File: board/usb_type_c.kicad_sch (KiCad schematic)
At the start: 3 parts, among them J1101 MOLEX_2171790001, U1101 DT1446-04V-7

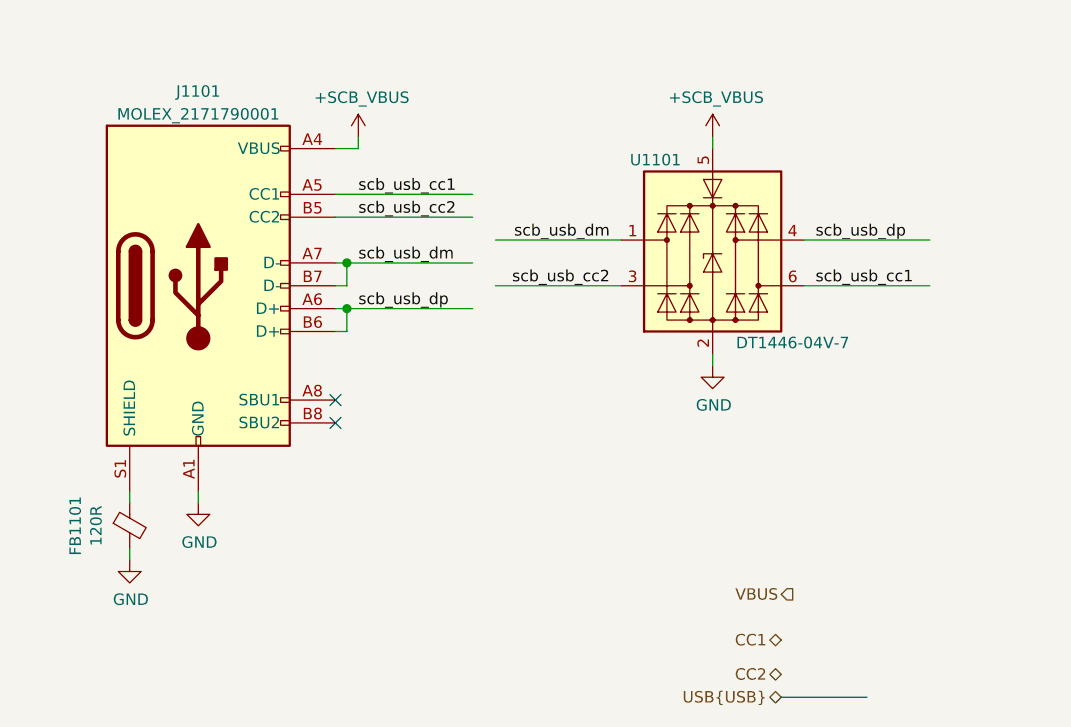
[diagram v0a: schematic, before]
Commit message: Added testpoints and other fixes
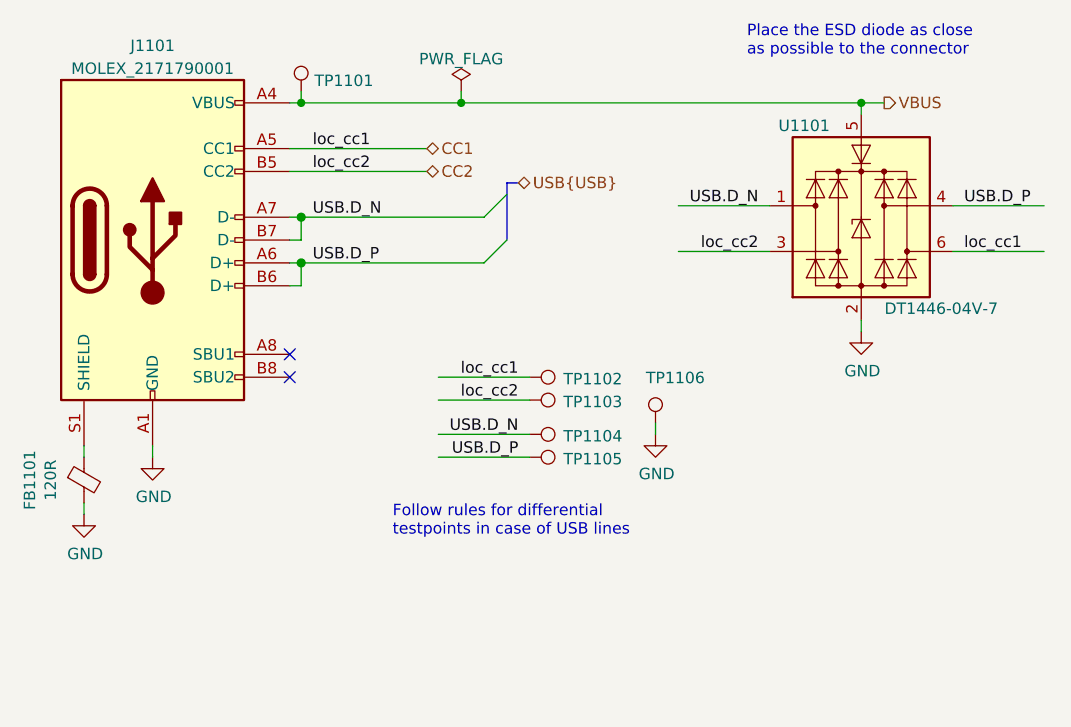
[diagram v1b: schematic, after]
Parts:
- added TP1101, TP1102, TP1103, TP1104, TP1105, TP1106: TestPoint, DIYPie:TestPoint_Pad_D1.5mm, symbol DIYPie:TestPoint
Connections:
- net +5V is gone; now on net VBUS: J1101.A4 (VBUS), J1101.A9 (VBUS), J1101.B4 (VBUS), J1101.B9 (VBUS), U1101.5 (VBUS)
- net scb_usb_cc1 is gone; now on net CC1: J1101.A5 (CC1), U1101.6 (I/O4)
- net scb_usb_cc2 is gone; now on net CC2: J1101.B5 (CC2), U1101.3 (I/O2)
- net CC1: now also TP1102.1
- net CC2: now also TP1103.1
- net GND: now also TP1106.1
- net VBUS: now also TP1101.1
- net scb_usb_dm renamed USB.D_N
- net USB.D_N: now also TP1104.1
- net scb_usb_dp renamed USB.D_P
- net USB.D_P: now also TP1105.1
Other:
- note added: "Follow rules for differential testpoints in case of USB lines"
- note added: "Place the ESD diode as close as possible to the connector"
- moved on the sheet: FB1101, J1101, U1101
